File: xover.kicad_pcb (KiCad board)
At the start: 2 copper layers, 100 x 100 mm, 192 parts, among them J1 Screw_Terminal_01x04, J10 Conn_02x03_Odd_Even, J11 Conn_02x03_Odd_Even, J12 Conn_02x03_Odd_Even, J13 Conn_02x03_Odd_Even, J14 Conn_02x03_Odd_Even, J2 Conn_02x03_Odd_Even, J3 Screw_Terminal_01x02, J4 Conn_02x03_Odd_Even, J5 Screw_Terminal_01x04, J6 Screw_Terminal_01x04, J7 Screw_Terminal_01x03, J8 Conn_02x03_Odd_Even, J9 Conn_01x04_Male, U1 NE5532, U10 NE5532, U11 NE5532, U12 NE5532, U13 NE5532, U2 NE5532, U3 NE5532, U4 NE5532, U5 NE5532, U6 NE5532, U7 NE5532, U8 NE5532, U9 NE5532

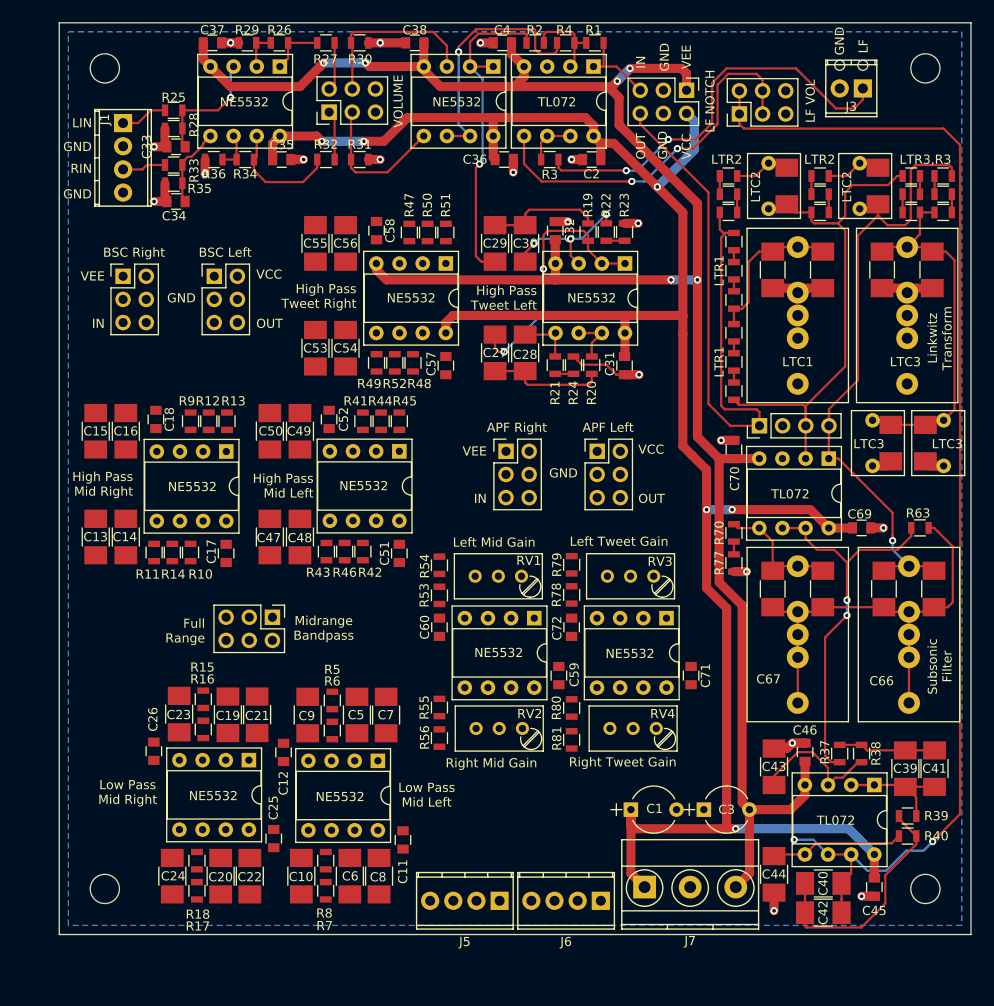
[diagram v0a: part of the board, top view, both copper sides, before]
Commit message: completed routing the crossover board
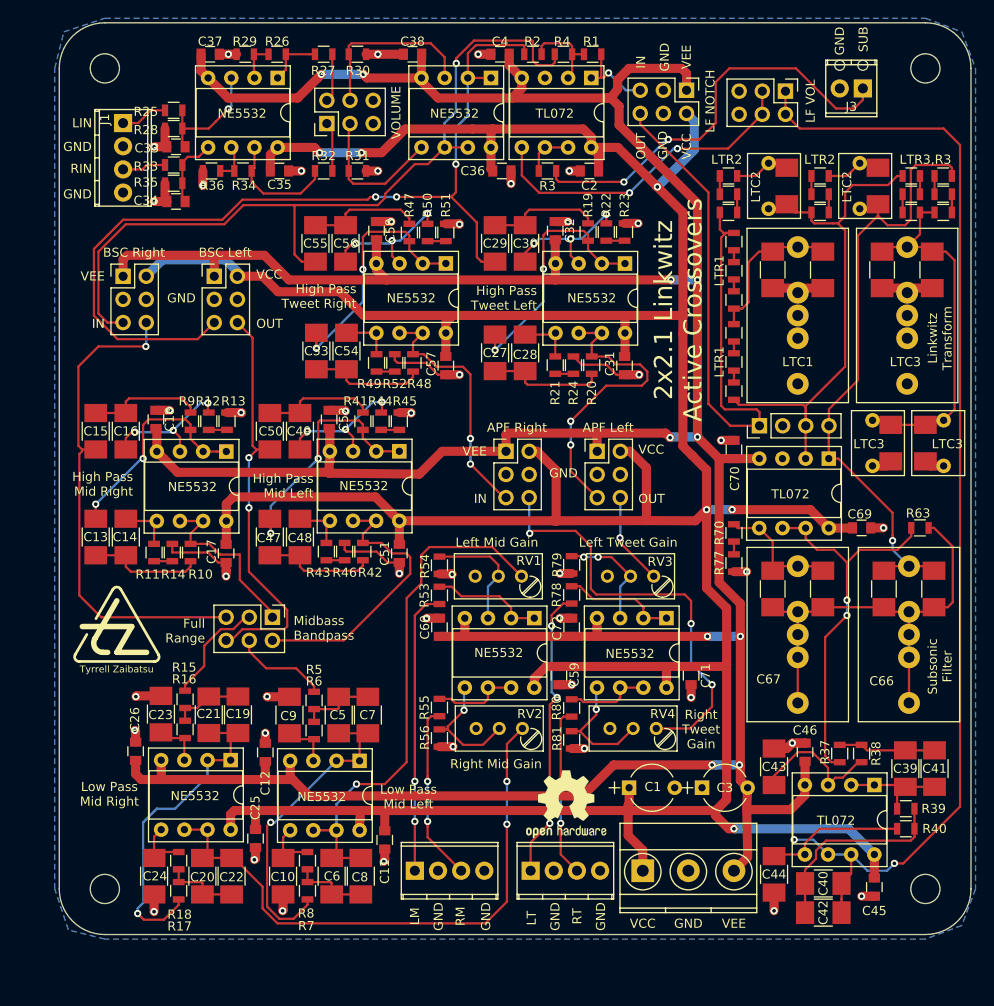
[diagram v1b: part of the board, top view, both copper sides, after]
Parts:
- added REF**: Tyrrell Zaibatsu, tz:Tyrrell-Zaibatsu-20-Back, F.Cu at (58.0, 93.0)
- added REF**: Tyrrell Zaibatsu, tz:Tyrrell-Zaibatsu-10, F.Cu at (31.3, 91.8)
- added REF***: OSHW-Logo2_9.8x8mm_SilkScreen, Symbols:OSHW-Logo2_9.8x8mm_SilkScreen, B.Cu at (34.0, 92.0)
- added REF***: OSHW-Logo2_9.8x8mm_SilkScreen, Symbols:OSHW-Logo2_9.8x8mm_SilkScreen, F.Cu at (80.6, 110.7)
- moved J5 9.87 mm to (64.0, 118.0), turned to 0 degrees
- moved J6 8.38 mm to (76.7, 118.0), turned to 0 degrees
- moved J2 5.63 mm to (104.7, 32.5), turned to 270 degrees
- moved C21 5.30 mm to (41.4, 100.9), turned to 90 degrees
- moved C1 2.41 mm to (87.5, 108.9)
- moved C3 2.41 mm to (95.5, 108.9)
- moved C10 2.00 mm to (49.5, 118.6)
- moved C11 2.00 mm to (60.7, 114.6)
- moved C12 2.00 mm to (47.6, 105.0)
- moved C20 2.00 mm to (40.7, 118.6)
- moved C22 2.00 mm to (43.9, 118.6)
- moved C23 2.00 mm to (36.1, 100.8)
- moved C24 2.00 mm to (35.4, 118.6)
- moved C25 2.00 mm to (46.5, 114.5)
- moved C26 2.00 mm to (33.4, 104.9)
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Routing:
- net VEE: track 220.3 -> 442.4 mm, vias 6 -> 10
- net VCC: track 230.3 -> 427.2 mm
- net /mid gain/IN2: track 0.00 -> 64.3 mm, vias 0 -> 2
- net /BSC L/IN: track 36.6 -> 100.4 mm, vias 1 -> 3
- net /BSC R/IN: track 27.8 -> 88.8 mm
- net GND: track 59.7 -> 120.2 mm, vias 19 -> 44
- net /mid gain/IN1: track 0.00 -> 57.5 mm, vias 0 -> 1
- net /HP mid R/IN: track 0.00 -> 54.9 mm, vias 0 -> 1
- net /tweet gain/IN2: track 0.00 -> 47.4 mm, vias 0 -> 3
- net /HP mid L/IN: track 0.00 -> 45.1 mm, vias 0 -> 2
- net /LP mid R/FB1: track 0.00 -> 36.3 mm, vias 0 -> 1
- net /LP mid L/FB1: track 0.00 -> 34.8 mm, vias 0 -> 1
- net /tweet gain/OUT1: track 0.00 -> 32.2 mm, vias 0 -> 4
- net /HP mid L/OUT: track 0.00 -> 31.4 mm
- net /mid gain/OUT1: track 0.00 -> 31.2 mm, vias 0 -> 2
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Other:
- outline, holes or cut-outs redrawn
- rule trace_min: 0.2 -> 0.25
- board text added: "2x2.1 Linkwitz Active Crossovers"
- board text added: "LM"
- board text added: "LT"
- board text added: "Midbass Bandpass"
- board text added: "RM"
- board text added: "RT"
- board text added: "Rev.A 202110 william@brodie-tyrrell.org github.com/phenidone"
- board text added: "SUB"
- board text removed: "LF"
- board text removed: "Midrange Bandpass"

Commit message: created gerbers
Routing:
- net /notch/IN: track 8.93 -> 9.60 mm, vias 1 -> 0
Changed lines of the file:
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@@
     (thickness 1.6)
     (drawings 89)
-    (tracks 1305)
+    (tracks 1303)
     (zones 0)
     (modules 196)
@@
       (outputformat 1)
       (mirror false)
-      (drillshape 1)
+      (drillshape 0)
       (scaleselection 1)
-      (outputdirectory ""))
+      (outputdirectory "plot"))
   )
   (net 0 "")
@@
   (segment (start 121 104.8) (end 117.8 104.8) (width 0.25) (layer F.Cu) (net 30))
   (segment (start 112.8 104.2) (end 113 104.2) (width 0.25) (layer F.Cu) (net 30))
-  (segment (start 110.6 106.1) (end 110.9 106.1) (width 0.25) (layer F.Cu) (net 68))
   (segment (start 113.6 104.8) (end 113 104.2) (width 0.25) (layer F.Cu) (net 30))
   (segment (start 117.8 104.8) (end 113.6 104.8) (width 0.25) (layer F.Cu) (net 30))
@@
   (segment (start 114.4 108.6) (end 117.6 108.6) (width 0.25) (layer F.Cu) (net 31))
   (segment (start 117.8 108.8) (end 121 108.8) (width 0.25) (layer F.Cu) (net 31))
-  (segment (start 106.8 121.1) (end 106.8 119.4) (width 0.25) (layer F.Cu) (net 32))
-  (segment (start 106.8 122.6) (end 106.8 121.1) (width 0.25) (layer F.Cu) (net 32))
   (segment (start 116.9 111.2) (end 116.9 111.5) (width 0.25) (layer F.Cu) (net 31))
   (segment (start 117.1 109.5) (end 117.8 108.8) (width 0.25) (layer F.Cu) (net 31))
   (segment (start 116.9 109.7) (end 117.8 108.8) (width 0.25) (layer F.Cu) (net 31))
   (segment (start 116.9 111.2) (end 116.9 109.7) (width 0.25) (layer F.Cu) (net 31))
+  (segment (start 106.8 121.1) (end 106.8 119.4) (width 0.25) (layer F.Cu) (net 32))
+  (segment (start 106.8 122.6) (end 106.8 121.1) (width 0.25) (layer F.Cu) (net 32))
   (segment (start 118.8 113.4) (end 118.8 111.2) (width 0.25) (layer F.Cu) (net 32))
   (segment (start 118.8 113.8) (end 118.8 113.4) (width 0.25) (layer F.Cu) (net 32))
@@
   (segment (start 85 64.8) (end 88.9 64.8) (width 0.25) (layer F.Cu) (net 67))
   (segment (start 81.1 68.7) (end 85 64.8) (width 0.25) (layer F.Cu) (net 67))
+  (segment (start 110.6 106.1) (end 110.9 106.1) (width 0.25) (layer F.Cu) (net 68))
   (segment (start 105.45137 80.42) (end 106.86 80.42) (width 0.25) (layer F.Cu) (net 68))
   (segment (start 104.32 80.42) (end 105.45137 80.42) (width 0.25) (layer F.Cu) (net 68))
@@
   (segment (start 84.45 31) (end 84.4 31.05) (width 0.25) (layer F.Cu) (net 73))
   (segment (start 84.45 28.45) (end 84.45 31) (width 0.25) (layer F.Cu) (net 73))
-  (via (at 85.25 30.5) (size 0.8) (drill 0.4) (layers F.Cu B.Cu) (net 73))
-  (segment (start 87.15 32.4) (end 85.25 30.5) (width 0.25) (layer B.Cu) (net 73))
   (segment (start 88.72 32.4) (end 87.15 32.4) (width 0.25) (layer B.Cu) (net 73))
-  (segment (start 84.75 31) (end 84.45 31) (width 0.25) (layer F.Cu) (net 73))
-  (segment (start 85.25 30.5) (end 84.75 31) (width 0.25) (layer F.Cu) (net 73))
+  (segment (start 85.8 31.05) (end 87.15 32.4) (width 0.25) (layer B.Cu) (net 73))
+  (segment (start 83.35 31.05) (end 85.8 31.05) (width 0.25) (layer B.Cu) (net 73))
   (segment (start 81.15 30.71) (end 80.81 31.05) (width 0.25) (layer F.Cu) (net 74))
   (segment (start 77.9 27.55) (end 78.2 27.25) (width 0.25) (layer F.Cu) (net 74))

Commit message: polished the layout and taped out
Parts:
- moved FID1 278.2 mm to (116.0, 27.0)
- moved FID4 253.2 mm to (123.0, 116.0)
- moved FID3 219.2 mm to (34.0, 27.0)
- moved FID2 157.6 mm to (27.0, 116.0)
- moved REF*** 73.1 mm to (56.6, 41.6)
- moved R32 11.5 mm to (52.6, 29.8), turned to 90 degrees
- moved R31 9.36 mm to (52.6, 33.4), turned to 270 degrees
- moved R27 6.93 mm to (60.8, 29.8), turned to 90 degrees
- moved J8 6.53 mm to (55.4, 29.6), turned to 0 degrees
- moved R30 5.84 mm to (60.8, 33.4), turned to 270 degrees
- moved J2 4.83 mm to (100.8, 29.6), turned to 0 degrees
- moved J14 4.40 mm to (90.4, 29.6), turned to 0 degrees
- moved R37 2.40 mm to (113.0, 105.2), turned to 90 degrees
- moved R38 2.40 mm to (110.6, 105.2), turned to 270 degrees
- moved C31 1.89 mm to (88.6, 61.6), turned to 180 degrees
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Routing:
- net VCC: track 427.2 -> 448.0 mm, vias 6 -> 5
- net Net-(R26-Pad1): track 6.17 -> 16.0 mm
- net Net-(J3-Pad1): track 45.9 -> 55.5 mm
- net Net-(J8-Pad3): track 16.0 -> 25.2 mm, vias 0 -> 2
- net /APF L/IN: track 33.3 -> 25.9 mm
- net /LP sub/VP1: track 15.6 -> 21.6 mm
- net VEE: track 442.4 -> 448.1 mm, vias 10 -> 8
- net Net-(J2-Pad3): track 36.3 -> 41.6 mm
- net /HP tweet R/FB1: track 28.1 -> 23.8 mm, vias 2 -> 1
- net /HP mid L/FB1: track 27.8 -> 23.7 mm, vias 2 -> 1
- net /HP tweet L/FB1: track 28.1 -> 24.1 mm, vias 2 -> 1
- net /LP sub/IN: track 42.8 -> 39.2 mm
- net /notch/IN: track 9.60 -> 12.3 mm
- net Net-(C33-Pad1): track 13.6 -> 11.0 mm
- net /LP mid R/FB1: track 36.3 -> 33.8 mm
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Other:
- board text added: "LPF LF"

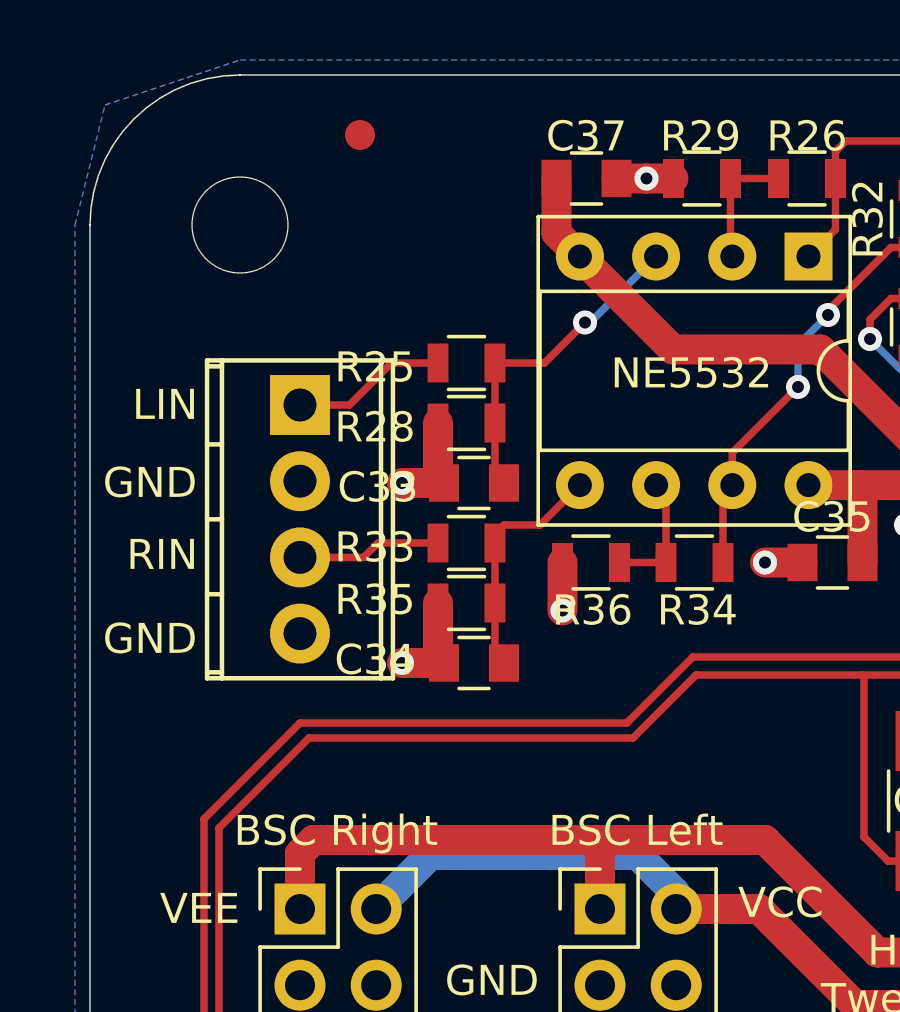
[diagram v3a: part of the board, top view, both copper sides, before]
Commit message: Rev.B adds "hum break resistor" in input network
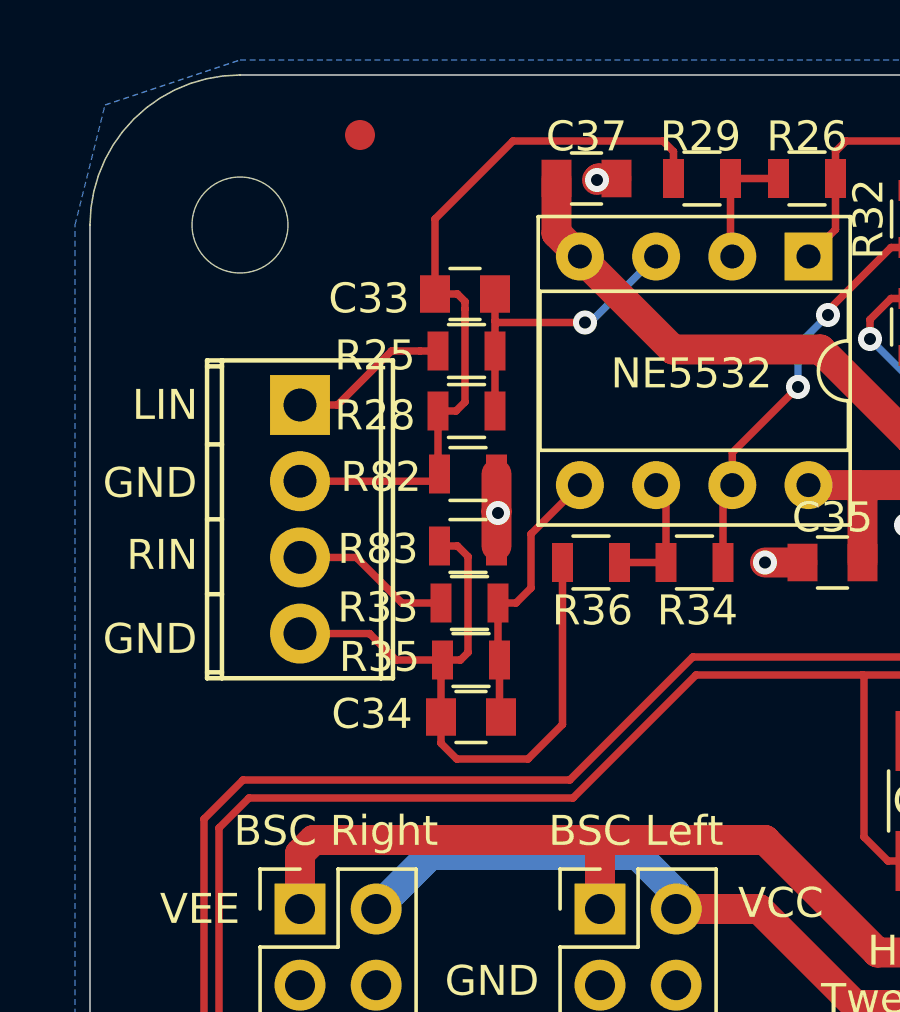
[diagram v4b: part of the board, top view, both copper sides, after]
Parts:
- added R82: 15, Resistors_SMD:R_0805, F.Cu at (37.6, 38.3)
- added R83: 15, Resistors_SMD:R_0805, F.Cu at (37.6, 40.7)
- R28, R35: value 33k -> 22k
- R30, R31: value 3k9 -> 1k8
- moved C33 6.31 mm to (37.5, 32.3)
- moved R33 2.00 mm to (37.6, 42.6)
- moved R35 1.91 mm to (37.7, 44.5)
- moved C34 1.80 mm to (37.7, 46.4)
- moved R25 0.40 mm to (37.5, 34.2)
- moved R28 0.40 mm to (37.5, 36.2)
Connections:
- net /BSC L/IN renamed /inbuf/OUT1
- net /BSC R/IN renamed /inbuf/OUT2
- C33 pad 2: GND -> /inbuf/IN1GND
- C34 pad 2: GND -> /inbuf/IN2GND
- J1 pad 2: GND -> /inbuf/IN1GND
- J1 pad 4: GND -> /inbuf/IN2GND
- R28 pad 2: GND -> /inbuf/IN1GND
- R29 pad 1: GND -> /inbuf/IN1GND
- R35 pad 2: GND -> /inbuf/IN2GND
- R36 pad 1: GND -> /inbuf/IN2GND
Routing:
- net /inbuf/IN1GND: track 0.00 -> 24.9 mm
- net /inbuf/IN2GND: track 0.00 -> 23.3 mm
- net GND: track 118.1 -> 110.7 mm, vias 45 -> 43
- net Net-(C34-Pad1): track 7.93 -> 9.55 mm
- net /inbuf/IN2: track 4.80 -> 5.33 mm
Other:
- board text added: "Rev.B 202201 william@brodie-tyrrell.org github.com/phenidone"
- board text removed: "Rev.A 202110 william@brodie-tyrrell.org github.com/phenidone"
